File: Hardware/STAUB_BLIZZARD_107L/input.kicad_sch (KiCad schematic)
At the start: 30 parts, among them IC2 MC33978AES

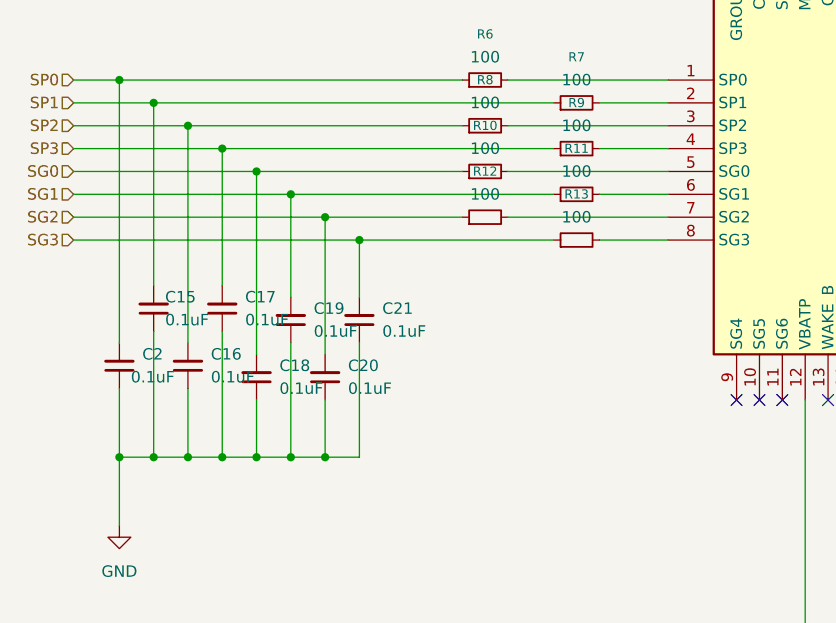
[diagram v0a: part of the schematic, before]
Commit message: Mise à jour du nom des pins dans le schématique et reprise du routage. Correction du PCB. Suppresion des SG inutilisés
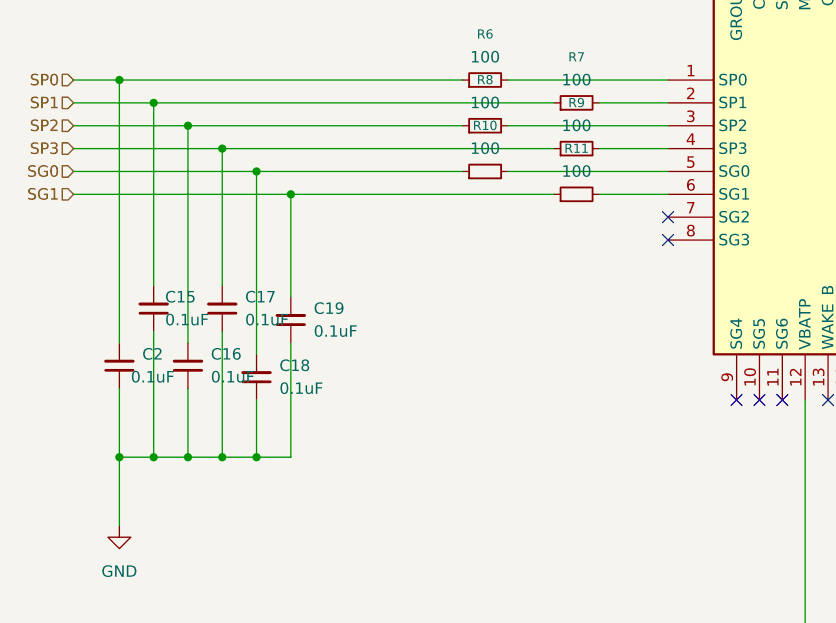
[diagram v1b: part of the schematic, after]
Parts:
- removed C20, C21: 0.1uF, Capacitor_SMD:C_0402_1005Metric, symbol Device:C_Small
- removed R12, R13: 100, Resistor_SMD:R_0603_1608Metric, symbol Device:R_Small
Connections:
- no-connect marks 11 -> 13
